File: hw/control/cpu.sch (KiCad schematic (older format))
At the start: 21 parts, among them J301 Conn_02x05_Odd_Even, J302 Conn_01x04, J303 Raspberry_Pi_0_2_3, J304 Micro_SD_Card, J305 Conn_01x06

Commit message: [hw] Assign SD Card holder footprint
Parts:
- J304: footprint (none) -> my:micro_sd_card
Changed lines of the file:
@@
 F 0 "J304" H 3150 7417 50  0000 C CNN
 F 1 "Micro_SD_Card" H 3150 7326 50  0000 C CNN
-F 2 "" H 4350 7000 50  0001 C CNN
+F 2 "my:micro_sd_card" H 4350 7000 50  0001 C CNN
 F 3 "http://katalog.we-online.de/em/datasheet/693072010801.pdf" H 3200 6700 50  0001 C CNN
 	1    3200 6700

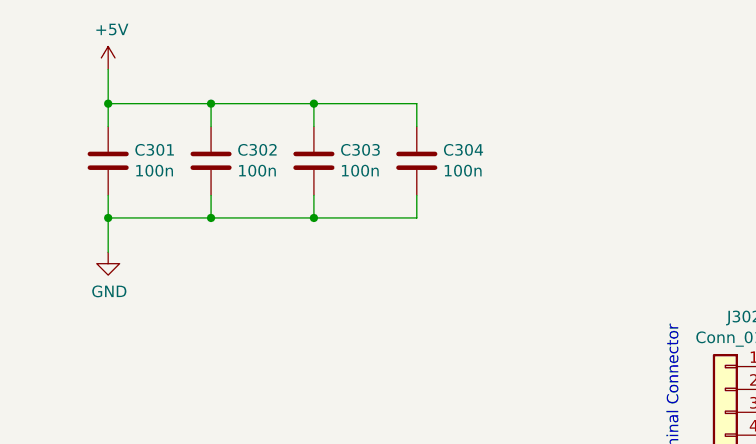
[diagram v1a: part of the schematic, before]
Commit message: [hw] Spread-out the components on control layout
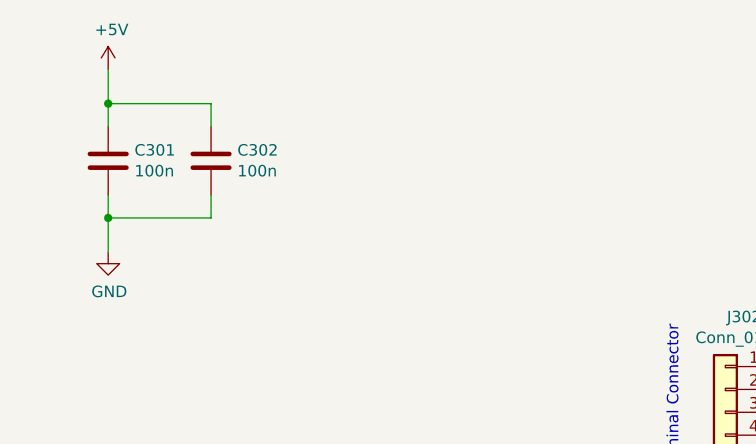
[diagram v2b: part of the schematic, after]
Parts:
- removed C303, C304: 100n, Capacitor_SMD:C_0805_2012Metric_Pad1.18x1.45mm_HandSolder, symbol Device:C
- J303: footprint Connector_PinHeader_2.54mm:PinHeader_2x20_P2.54mm_Vertical -> Module:Raspberry_Pi_Zero_Socketed_THT_FaceDown_MountingHoles
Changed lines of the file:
@@
-$EndComp
-$Comp
-L Device:C C303
-U 1 1 61471600
-P 1850 1200
-F 0 "C303" H 1965 1246 50  0000 L CNN
-F 1 "100n" H 1965 1155 50  0000 L CNN
-F 2 "Capacitor_SMD:C_0805_2012Metric_Pad1.18x1.45mm_HandSolder" H 1888 1050 50  0001 C CNN
-F 3 "~" H 1850 1200 50  0001 C CNN
-	1    1850 1200
-	1    0    0    -1
-$EndComp
-$Comp
-L Device:C C304
-U 1 1 61472029
-P 2300 1200
-F 0 "C304" H 2415 1246 50  0000 L CNN
-F 1 "100n" H 2415 1155 50  0000 L CNN
-F 2 "Capacitor_SMD:C_0805_2012Metric_Pad1.18x1.45mm_HandSolder" H 2338 1050 50  0001 C CNN
-F 3 "~" H 2300 1200 50  0001 C CNN
-	1    2300 1200
-	1    0    0    -1
 $EndComp
 $Comp
@@
 	950  1450 950  1350
 Wire Wire Line
-	1400 1450 1850 1450
-Wire Wire Line
-	1850 1450 1850 1350
-Connection ~ 1400 1450
-Wire Wire Line
-	1850 1450 2300 1450
-Wire Wire Line
-	2300 1450 2300 1350
-Connection ~ 1850 1450
-Wire Wire Line
 	950  800  950  950
 Wire Wire Line
@@
 Wire Wire Line
 	950  950  950  1050
-Wire Wire Line
-	1400 950  1850 950
-Wire Wire Line
-	1850 950  1850 1050
-Connection ~ 1400 950
-Wire Wire Line
-	1850 950  2300 950
-Wire Wire Line
-	2300 950  2300 1050
-Connection ~ 1850 950
 $Comp
 L my:Raspberry_Pi_0_2_3 J303
@@
 F 0 "J303" H 6900 2250 50  0000 C CNN
 F 1 "Raspberry_Pi_0_2_3" H 7200 2350 50  0000 C CNN
-F 2 "Connector_PinHeader_2.54mm:PinHeader_2x20_P2.54mm_Vertical" H 6500 3650 50  0001 C CNN
+F 2 "Module:Raspberry_Pi_Zero_Socketed_THT_FaceDown_MountingHoles" H 6500 3650 50  0001 C CNN
 F 3 "https://www.raspberrypi.org/documentation/hardware/raspberrypi/schematics/rpi_SCH_3bplus_1p0_reduced.pdf" H 6500 3650 50  0001 C CNN
 	1    6500 3650

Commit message: [hw] Add control board net classes
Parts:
- J303: footprint Module:Raspberry_Pi_Zero_Socketed_THT_FaceDown_MountingHoles -> my:Raspberry_Pi_Zero_Socketed_THT_FaceDown_MountingHoles_No_Courtyard
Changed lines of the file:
@@
 F 0 "J303" H 6900 2250 50  0000 C CNN
 F 1 "Raspberry_Pi_0_2_3" H 7200 2350 50  0000 C CNN
-F 2 "Module:Raspberry_Pi_Zero_Socketed_THT_FaceDown_MountingHoles" H 6500 3650 50  0001 C CNN
+F 2 "my:Raspberry_Pi_Zero_Socketed_THT_FaceDown_MountingHoles_No_Courtyard" H 6500 3650 50  0001 C CNN
 F 3 "https://www.raspberrypi.org/documentation/hardware/raspberrypi/schematics/rpi_SCH_3bplus_1p0_reduced.pdf" H 6500 3650 50  0001 C CNN
 	1    6500 3650

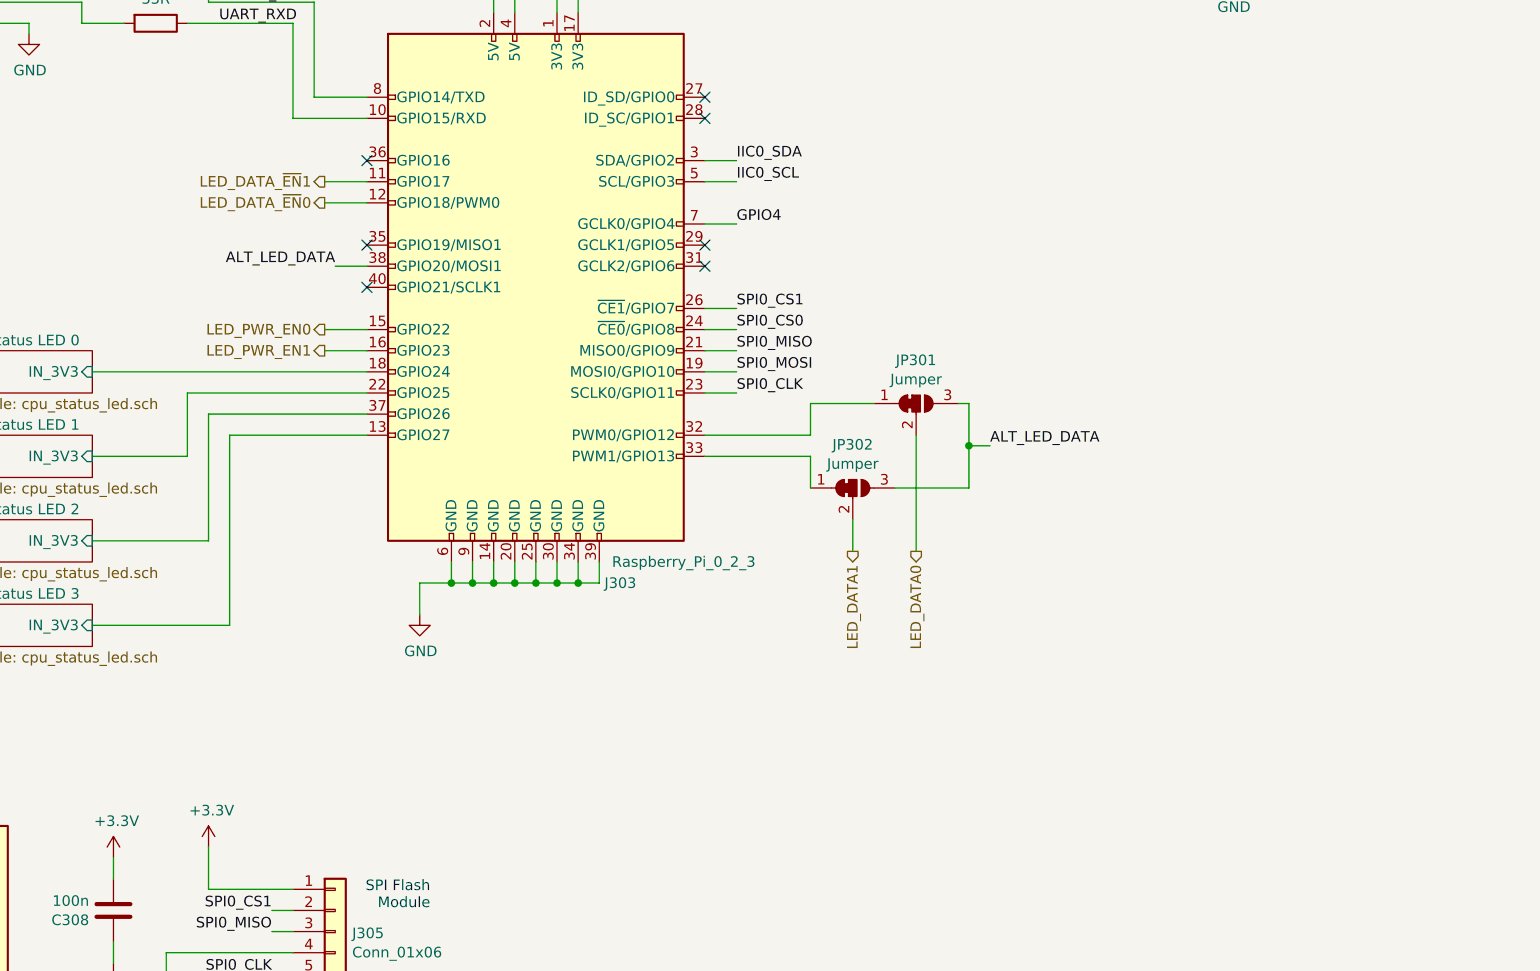
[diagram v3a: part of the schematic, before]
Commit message: i[hw] Add IIS audio module connector
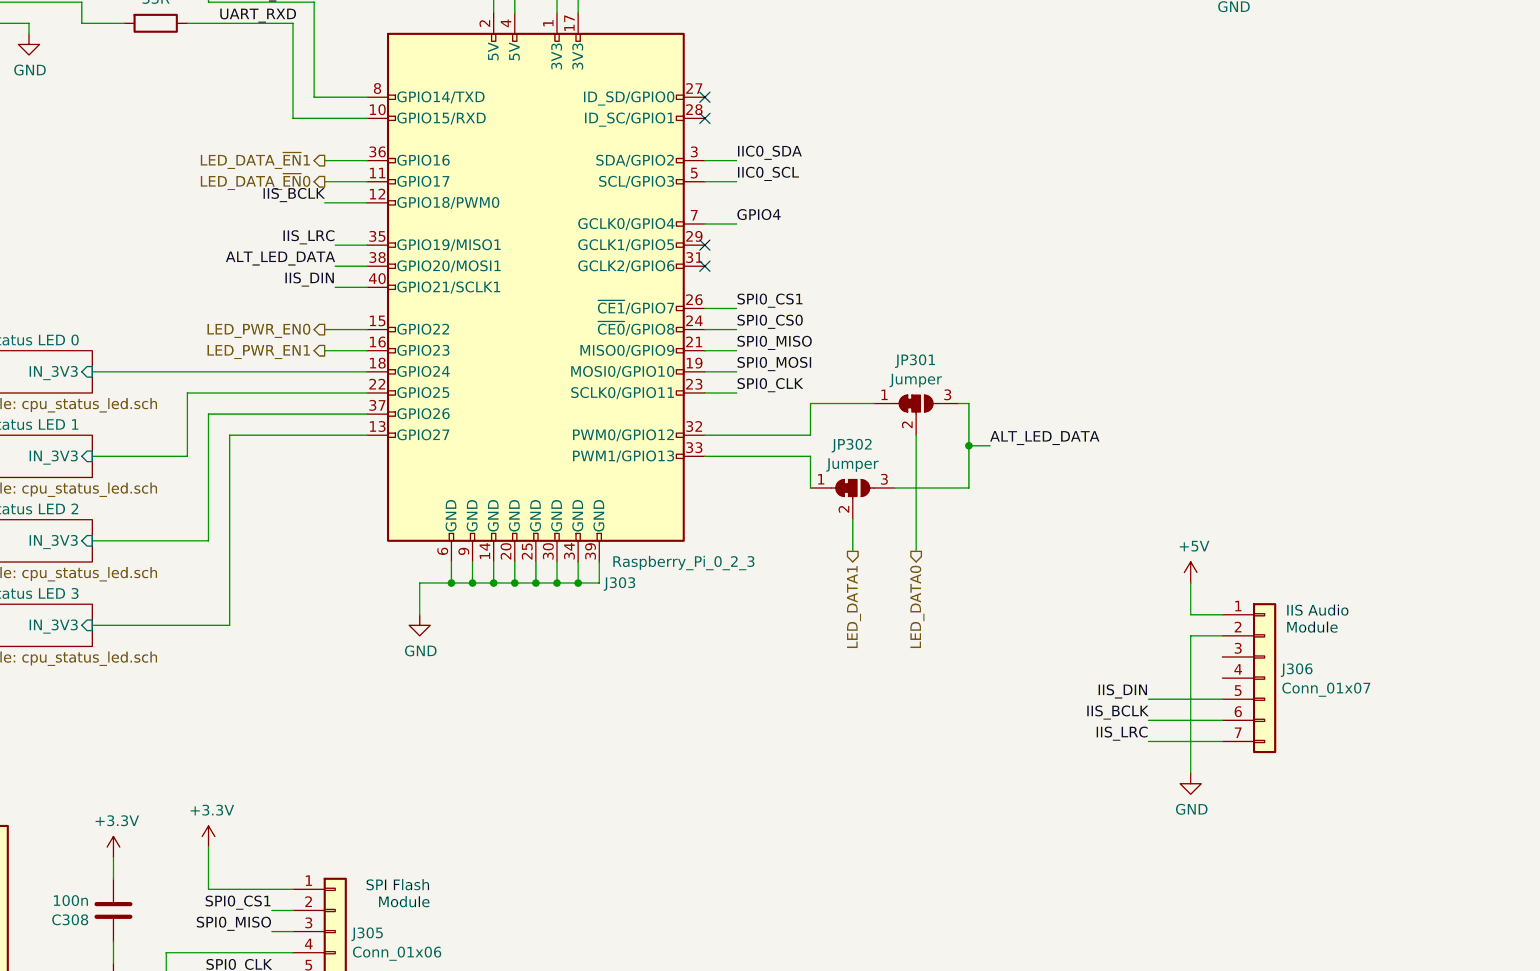
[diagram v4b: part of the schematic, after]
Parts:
- added J306: Conn_01x07, Connector_PinHeader_2.54mm:PinHeader_1x07_P2.54mm_Vertical, symbol Connector_Generic:Conn_01x07
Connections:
- net +5V: now also J306.1 (Pin_1)
- net GND: now also J306.2 (Pin_2)
- net LED_DATA_~EN~0: now also J303.11 (GPIO17); no longer J303.12 (GPIO18/PWM0)
- net LED_DATA_~EN~1: now also J303.36 (GPIO16); no longer J303.11 (GPIO17)
- net IIS_LRC: now reaches J303.35 (GPIO19/MISO1)
- net IIS_LRC: now also J306.7 (Pin_7)
- net IIS_DIN: now reaches J303.40 (GPIO21/SCLK1)
- net IIS_DIN: now also J306.5 (Pin_5)
- new net IIS_BCLK: J303.12 (GPIO18/PWM0), J306.6 (Pin_6)
- no-connect marks 9 -> 6
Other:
- note added: "IIS Audio\nModule"
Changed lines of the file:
@@
 NoConn ~ 7300 3450
 NoConn ~ 7300 3550
-Text HLabel 5500 3250 0    50   Output ~ 0
+Text HLabel 5500 3150 0    50   Output ~ 0
 LED_DATA_~EN~0
 Wire Wire Line
-	5500 3250 5700 3250
-Text HLabel 5500 3150 0    50   Output ~ 0
+	5500 3150 5700 3150
+Text HLabel 5500 3050 0    50   Output ~ 0
 LED_DATA_~EN~1
 Wire Wire Line
-	5500 3150 5700 3150
+	5500 3050 5700 3050
 Text Label 5550 3550 2    50   ~ 0
 ALT_LED_DATA
@@
 Wire Wire Line
 	8550 4400 8650 4400
-NoConn ~ 5700 3650
-NoConn ~ 5700 3450
 Wire Wire Line
 	7800 4350 7800 4200
@@
 Wire Wire Line
 	7300 4450 7800 4450
-NoConn ~ 5700 3050
 Text Notes 3450 2600 1    50   ~ 0
 Terminal Connector
@@
 Wire Wire Line
 	10850 1250 10850 1350
+$Comp
+L Connector_Generic:Conn_01x07 J306
+U 1 1 6182094F
+P 9950 5500
+F 0 "J306" H 10030 5542 50  0000 L CNN
+F 1 "Conn_01x07" H 10030 5451 50  0000 L CNN
+F 2 "Connector_PinHeader_2.54mm:PinHeader_1x07_P2.54mm_Vertical" H 9950 5500 50  0001 C CNN
+F 3 "~" H 9950 5500 50  0001 C CNN
+	1    9950 5500
+	1    0    0    -1
+$EndComp
+$Comp
+L power:+5V #PWR0323
+U 1 1 61827B3D
+P 9600 5050
+F 0 "#PWR0323" H 9600 4900 50  0001 C CNN
+F 1 "+5V" H 9615 5223 50  0000 C CNN
+F 2 "" H 9600 5050 50  0001 C CNN
+F 3 "" H 9600 5050 50  0001 C CNN
+	1    9600 5050
+	1    0    0    -1
+$EndComp
+$Comp
+L power:GND #PWR0324
+U 1 1 61828829
+P 9600 5950
+F 0 "#PWR0324" H 9600 5700 50  0001 C CNN
+F 1 "GND" H 9605 5777 50  0000 C CNN
+F 2 "" H 9600 5950 50  0001 C CNN
+F 3 "" H 9600 5950 50  0001 C CNN
+	1    9600 5950
+	1    0    0    -1
+$EndComp
+Wire Wire Line
+	9600 5950 9600 5300
+Wire Wire Line
+	9600 5300 9750 5300
+Wire Wire Line
+	9600 5050 9600 5200
+Wire Wire Line
+	9600 5200 9750 5200
+Wire Wire Line
+	9750 5600 9400 5600
+Wire Wire Line
+	9750 5700 9400 5700
+Wire Wire Line
+	9750 5800 9400 5800
+Text Label 9400 5800 2    50   ~ 0
+IIS_LRC
+Text Label 9400 5700 2    50   ~ 0
+IIS_BCLK
+Text Label 9400 5600 2    50   ~ 0
+IIS_DIN
+Text Notes 10050 5300 0    50   ~ 0
+IIS Audio\nModule
+Wire Wire Line
+	5700 3450 5550 3450
+Text Label 5550 3450 2    50   ~ 0
+IIS_LRC
+Wire Wire Line
+	5700 3250 5500 3250
+Text Label 5500 3250 2    50   ~ 0
+IIS_BCLK
+Wire Wire Line
+	5700 3650 5550 3650
+Text Label 5550 3650 2    50   ~ 0
+IIS_DIN
 $EndSCHEMATC

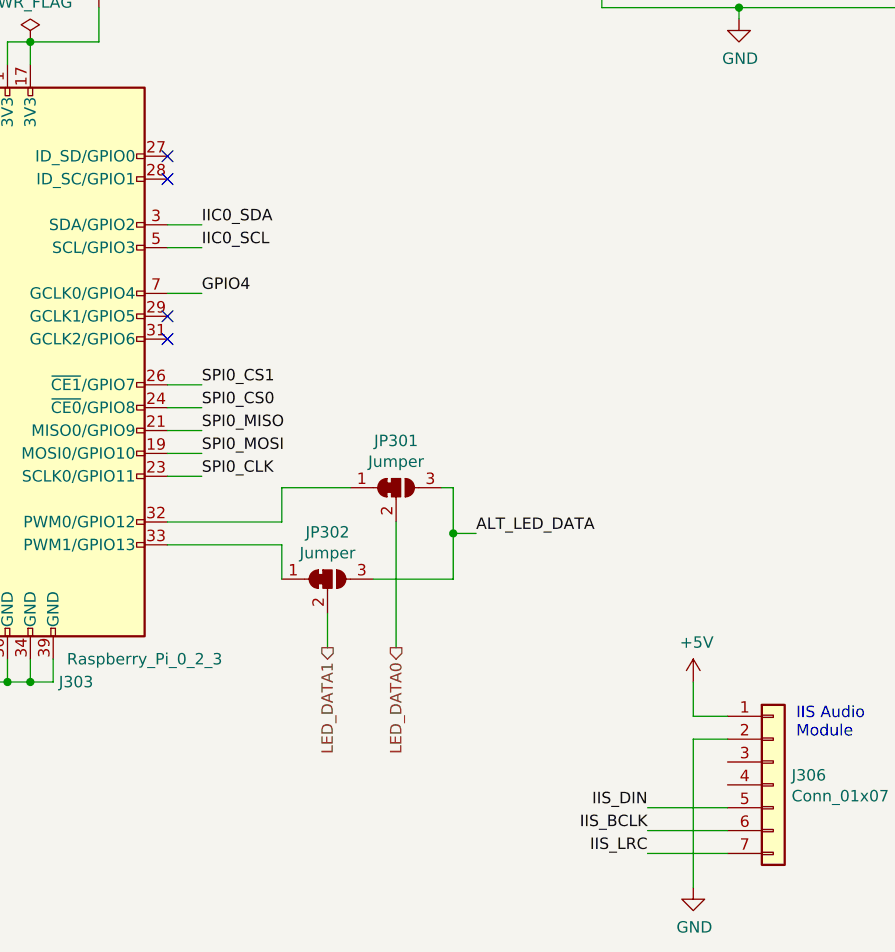
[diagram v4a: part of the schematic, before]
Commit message: [hw] Add button, move sd card
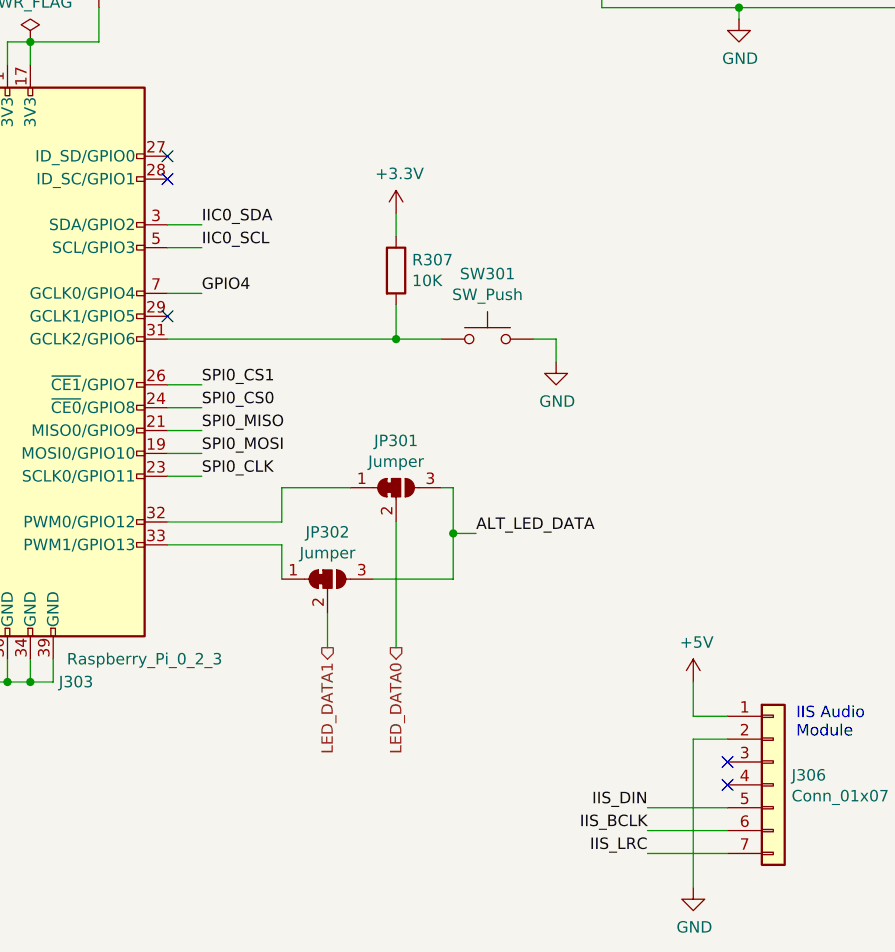
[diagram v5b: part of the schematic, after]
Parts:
- added R307: 10K, Resistor_SMD:R_0805_2012Metric_Pad1.20x1.40mm_HandSolder, symbol Device:R
- added SW301: SW_Push, Button_Switch_THT:SW_PUSH_6mm, symbol Switch:SW_Push
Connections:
- net +3V3: now also R307.1
- net GND: now also SW301.2
- net at J303.31 (GCLK2/GPIO6): now also R307.2, SW301.1
- no-connect marks 6 -> 7
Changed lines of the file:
@@
 NoConn ~ 7300 2850
 NoConn ~ 7300 3450
-NoConn ~ 7300 3550
 Text HLabel 5500 3150 0    50   Output ~ 0
 LED_DATA_~EN~0
@@
 Text Label 5550 3650 2    50   ~ 0
 IIS_DIN
+NoConn ~ 9750 5400
+NoConn ~ 9750 5500
+$Comp
+L Switch:SW_Push SW301
+U 1 1 618C6A0D
+P 8700 3550
+F 0 "SW301" H 8700 3835 50  0000 C CNN
+F 1 "SW_Push" H 8700 3744 50  0000 C CNN
+F 2 "Button_Switch_THT:SW_PUSH_6mm" H 8700 3750 50  0001 C CNN
+F 3 "~" H 8700 3750 50  0001 C CNN
+	1    8700 3550
+	1    0    0    -1
+$EndComp
+$Comp
+L power:+3.3V #PWR0325
+U 1 1 618C7D00
+P 8300 3000
+F 0 "#PWR0325" H 8300 2850 50  0001 C CNN
+F 1 "+3.3V" H 8315 3173 50  0000 C CNN
+F 2 "" H 8300 3000 50  0001 C CNN
+F 3 "" H 8300 3000 50  0001 C CNN
+	1    8300 3000
+	1    0    0    -1
+$EndComp
+$Comp
+L Device:R R307
+U 1 1 618C8EC8
+P 8300 3250
+F 0 "R307" H 8370 3296 50  0000 L CNN
+F 1 "10K" H 8370 3205 50  0000 L CNN
+F 2 "Resistor_SMD:R_0805_2012Metric_Pad1.20x1.40mm_HandSolder" V 8230 3250 50  0001 C CNN
+F 3 "~" H 8300 3250 50  0001 C CNN
+	1    8300 3250
+	1    0    0    -1
+$EndComp
+Wire Wire Line
+	8300 3000 8300 3100
+Wire Wire Line
+	8300 3400 8300 3550
+Wire Wire Line
+	8300 3550 8500 3550
+Wire Wire Line
+	7300 3550 8300 3550
+Connection ~ 8300 3550
+$Comp
+L power:GND #PWR0326
+U 1 1 618F59EF
+P 9000 3650
+F 0 "#PWR0326" H 9000 3400 50  0001 C CNN
+F 1 "GND" H 9005 3477 50  0000 C CNN
+F 2 "" H 9000 3650 50  0001 C CNN
+F 3 "" H 9000 3650 50  0001 C CNN
+	1    9000 3650
+	1    0    0    -1
+$EndComp
+Wire Wire Line
+	8900 3550 9000 3550
+Wire Wire Line
+	9000 3550 9000 3650
 $EndSCHEMATC
